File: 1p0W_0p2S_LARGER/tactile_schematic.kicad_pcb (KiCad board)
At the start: 2 copper layers, 145.2 x 85.6 mm, 55 parts, among them IC1 CY8C4145PVI-PS431, J1 Conn_01x03, J2 Conn_01x04, J3 Conn_01x04, J4 Conn_01x03, J5 Conn_ARM_SWD_TagConnect_TC203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

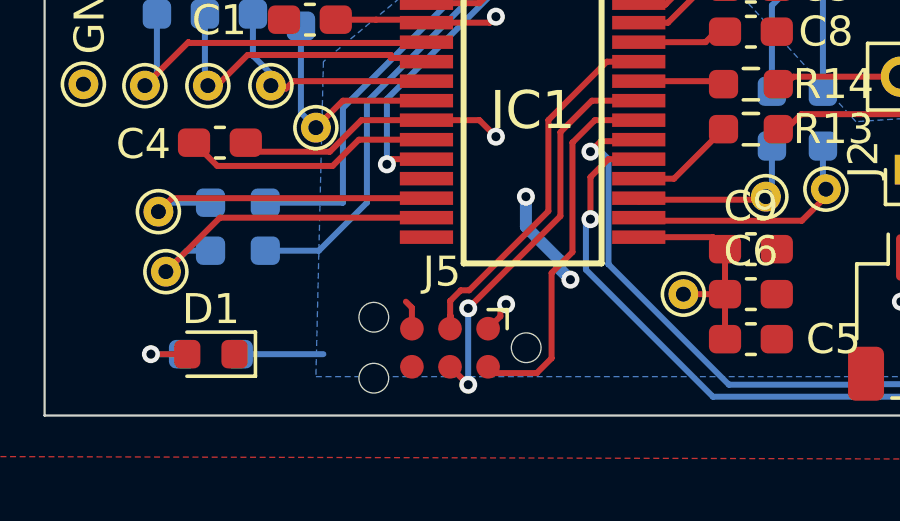
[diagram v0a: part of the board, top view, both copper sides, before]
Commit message: move prog connector up, make bottom of gnd plane connected propelrly
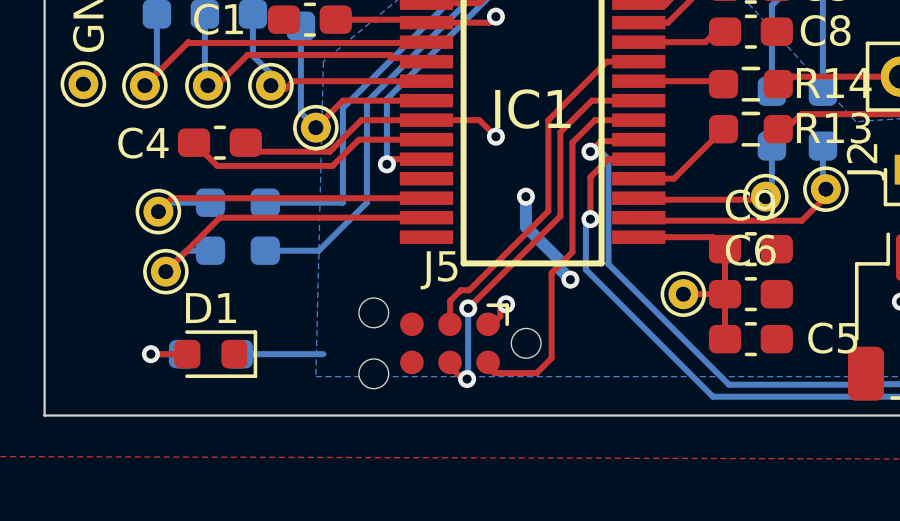
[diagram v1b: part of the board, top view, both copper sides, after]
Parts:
- moved J5 0.15 mm to (111.5, 126.9)
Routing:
- net GND: track 25.4 -> 24.4 mm
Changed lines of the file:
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@@
 	(footprint "Connector:Tag-Connect_TC2030-IDC-NL_2x03_P1.27mm_Vertical"
 		(layer "F.Cu")
-		(at 111.545603 127.031125 180)
+		(at 111.545603 126.885 180)
 		(descr "Tag-Connect programming header; http://www.tag-connect.com/Materials/TC2030-IDC-NL.pdf")
 		(tags "tag connect programming header pogo pins")
@@
 			(polygon
 				(pts
-					(xy 110.275603 127.666125) (xy 112.815603 127.666125) (xy 112.815603 126.396125) (xy 110.275603 126.396125)
+					(xy 110.275603 127.52) (xy 112.815603 127.52) (xy 112.815603 126.25) (xy 110.275603 126.25)
 				)
 			)
@@
 	)
 	(segment
-		(start 110.275603 125.696125)
-		(end 110.075603 125.496125)
-		(width 0.2)
-		(layer "F.Cu")
-		(net 2)
-	)
-	(segment
 		(start 108.508389 120.096125)
 		(end 107.632389 120.972125)
@@
 		(net 2)
 	)
-	(segment
-		(start 110.275603 126.396125)
-		(end 110.275603 125.696125)
-		(width 0.2)
-		(layer "F.Cu")
-		(net 2)
-	)
 	(via
 		(at 114.075603 121.996125)
@@
 	)
 	(segment
-		(start 111.55329 127.666125)
-		(end 112.152973 128.265808)
+		(start 111.963474 128.076309)
+		(end 111.55329 127.666125)
 		(width 0.2)
 		(layer "F.Cu")
@@
 	)
 	(segment
+		(start 112.116157 128.076309)
+		(end 111.963474 128.076309)
+		(width 0.2)
+		(layer "F.Cu")
+		(net 22)
+	)
+	(segment
 		(start 115.226603 119.845125)
 		(end 116.275603 118.796125)
@@
 	)
 	(segment
-		(start 112.152973 125.718755)
-		(end 115.226603 122.645125)
+		(start 111.55329 127.666125)
+		(end 111.545603 127.666125)
 		(width 0.2)
 		(layer "F.Cu")
@@
 	)
 	(segment
-		(start 111.545603 127.666125)
-		(end 111.55329 127.666125)
+		(start 112.152973 125.718755)
+		(end 115.226603 122.645125)
 		(width 0.2)
 		(layer "F.Cu")
@@
 	)
 	(via
-		(at 112.152973 128.265808)
+		(at 112.116157 128.076309)
 		(size 0.6)
 		(drill 0.3)
@@
 	)
 	(segment
-		(start 112.152973 125.718755)
-		(end 112.152973 128.265808)
+		(start 112.152973 128.047027)
+		(end 112.152973 125.718755)
+		(width 0.2)
+		(layer "B.Cu")
+		(net 22)
+	)
+	(segment
+		(start 112.116157 128.076309)
+		(end 112.123691 128.076309)
+		(width 0.2)
+		(layer "B.Cu")
+		(net 22)
+	)
+	(segment
+		(start 112.123691 128.076309)
+		(end 112.152973 128.047027)
 		(width 0.2)
 		(layer "B.Cu")
